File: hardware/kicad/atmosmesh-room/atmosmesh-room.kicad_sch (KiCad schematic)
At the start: 27 parts, among them U1 IDEASPARK_30PIN_PROVISIONAL

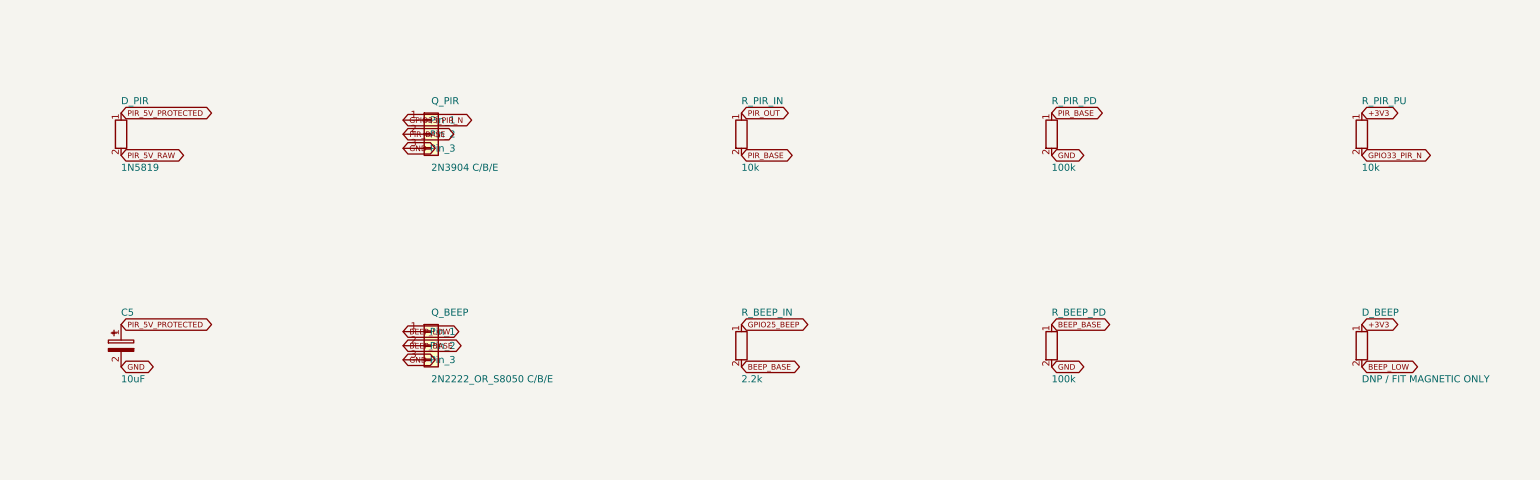
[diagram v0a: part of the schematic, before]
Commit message: :bug: fix(room): make the polarity symbols survive their own gates
The independent review asked for real polarity and C/B/E semantics so ERC can
catch a reversed diode or transistor. Fitting D_Schottky, D and Q_NPN_CBE and
adding per-instance descriptions did that, but left three gates red:

- The local library and the schematic's embedded copy were built from separate
  sources and given different Description text, so all 27 symbols raised
  lib_symbol_mismatch. Both now derive from the one list the schematic embeds,
  which also carries U1's passive pin types across.
- D_BEEP's new anode marker sits 7.62 mm right of the part origin and clipped
  mounting hole H2's mask at x=168. Moved to x=163.
- The .kicad_mod writer indents with spaces, so appending a literal tab to the
  marker continuation lines produced "space before tab" and failed task check.
  Continuation lines now extend the caller's own indent character.

Gates: ERC 0 violations, DRC 0 violations and 0 schematic-parity problems,
structural validation PASS, git diff --check clean. The 52 unconnected items
remain the intentional unrouted ratsnest. generate_project.py reproduces every
artifact byte-identically.
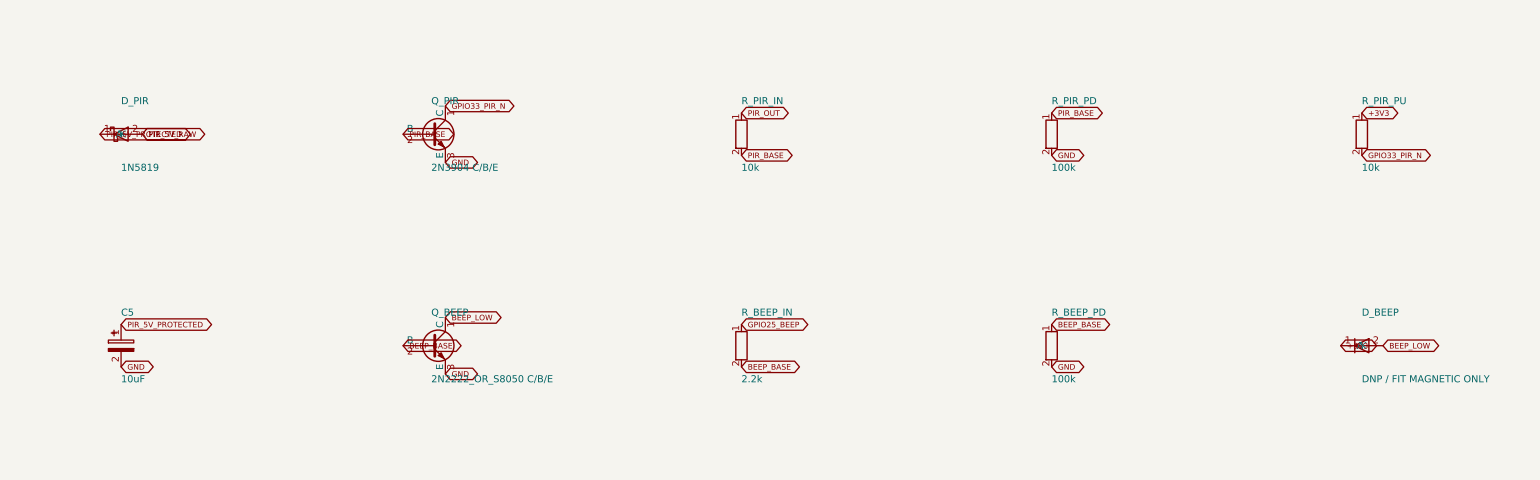
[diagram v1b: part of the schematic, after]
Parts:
- D_BEEP: symbol atmosmesh:R -> atmosmesh:D
- D_PIR: symbol atmosmesh:R -> atmosmesh:D_Schottky
- Q_BEEP, Q_PIR: symbol atmosmesh:Conn_01x03 -> atmosmesh:Q_NPN_CBE

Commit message: :sparkles: feat(room): build against the board the operator actually has
The controller is the ideaspark ESP32 1.14 inch TFT LCD board, confirmed from
docs/hardware/ideaspark-esp32-tft-pinout.png. The design assumed an integrated
I2C OLED, and that assumption was load-bearing in three places.

Its display is SPI. GPIO21/22 carry no onboard device, so:

- D-022's rejection of a sensor-supply diode rested on the OLED holding SDA/SCL
  at 3.3 V. That reason was false here. The decision is unchanged, on the real
  reason: every pull-up references the same rail the sensors run from.
- Nothing pulls the bus up. D-023 adds R_PU_SDA/R_PU_SCL 4k7 as required parts,
  on the sensor side of the 330R series resistors.
- GPIO23/18/15/2/4/32 belong to the display, GPIO12 is the flash strap and
  GPIO1/3 are the USB-UART. D-024 puts them off-limits behind a generator guard
  and a validator assertion.

U1's socket map was provisional and wrong in almost every position: pad 7 held
GPIO33 where the board has GPIO26, pad 30 held 3V3 where the board has GPIO23.
Rebuilt from a named pin table. Knowing the pin order makes the socket more
dangerous, not less, so the reserved pins are silkscreened too.

Operator also confirmed two module orders that were wrong on the carrier:

- SHT41 is VIN/GND/SCL/SDA; the carrier had SDA and SCL crossed.
- D-SUN PIR is GND/OUT/VCC; the carrier order would have put 5 V on the
  module's ground pin.

Gates: ERC 0, DRC 0 violations and 0 parity problems, structural validation
PASS, git diff --check clean. Both new gates mutation-proved: mapping GPIO23
raises in the generator, a rogue GPIO18 net fails the validator, and dropping
R_PU_SDA fails the pull-up assertion.

Still unverified: the physical row spacing, and both 5 V modules' supply
voltage and output swing.
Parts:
- added R_PU_SCL, R_PU_SDA: 4.7k, room:R_Axial_P7.62mm, symbol atmosmesh:R
- J_PIR: value DSUN_PIR -> DSUN_PIR GND/OUT/VCC
- J_SHT: value SHT41_3V3 -> SHT41 VIN/GND/SCL/SDA
- U1: value IDEASPARK_30PIN_PROVISIONAL -> IDEASPARK_ESP32_1V14_TFT_30PIN
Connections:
- net +3V3: now also U1.16 (GPIO23), R_PU_SCL.2, R_PU_SDA.2; no longer U1.30 (3V3)
- net +5V_USB_CONFIRMED: now also U1.1 (EN); no longer U1.15 (VIN)
- net GND: now also J_PIR.1 (Pin_1), U1.17 (GPIO22), U1.2 (GPIO36/VP); no longer J_PIR.2 (Pin_2), U1.14 (GND), U1.29 (GND)
- net GPIO21_SDA: now also U1.26 (GPIO4); no longer U1.20 (GPIO21)
- net GPIO22_SCL: now also U1.29 (GND); no longer U1.17 (GPIO22)
- net GPIO33_PIR_N: now also U1.9 (GPIO26); no longer U1.7 (GPIO33)
- net PIR_5V_PROTECTED: now also J_PIR.3 (Pin_3); no longer J_PIR.1 (Pin_1)
- net PIR_OUT: now also J_PIR.2 (Pin_2); no longer J_PIR.3 (Pin_3)
- net SCL_EXT: now also J_SHT.3 (Pin_3), R_PU_SCL.1; no longer J_SHT.4 (Pin_4)
- net SDA_EXT: now also J_SHT.4 (Pin_4), R_PU_SDA.1; no longer J_SHT.3 (Pin_3)
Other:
- note added: "DO NOT FABRICATE - IDEASPARK PIN NAMES CONFIRMED; ROW SPACING + MODULE PINOUTS STILL UNVERIFIED"
- note added: "Display is SPI, not I2C: GPIO21/22 carry no onboard device. R_PU_SDA/R_PU_SCL 4k7 are the only bus pullups."
- note added: "NEVER WIRE: GPIO23/18/15/2/4/32 drive the 1.14in TFT; GPIO12 is the flash strap; GPIO1/3 are the USB-UART."
- note removed: "DO NOT FABRICATE - VERIFY EXACT IDEASPARK BOARD / 30-PIN ROW SPACING / FRONT + BACK PHOTOS"
- note removed: "Onboard OLED stays directly on GPIO21/GPIO22. External sensors are behind 330R series resistors."
- moved on the sheet: C1, C2, C3, C4, TP_3V3, TP_5V, TP_GND, TP_SCL, TP_SDA

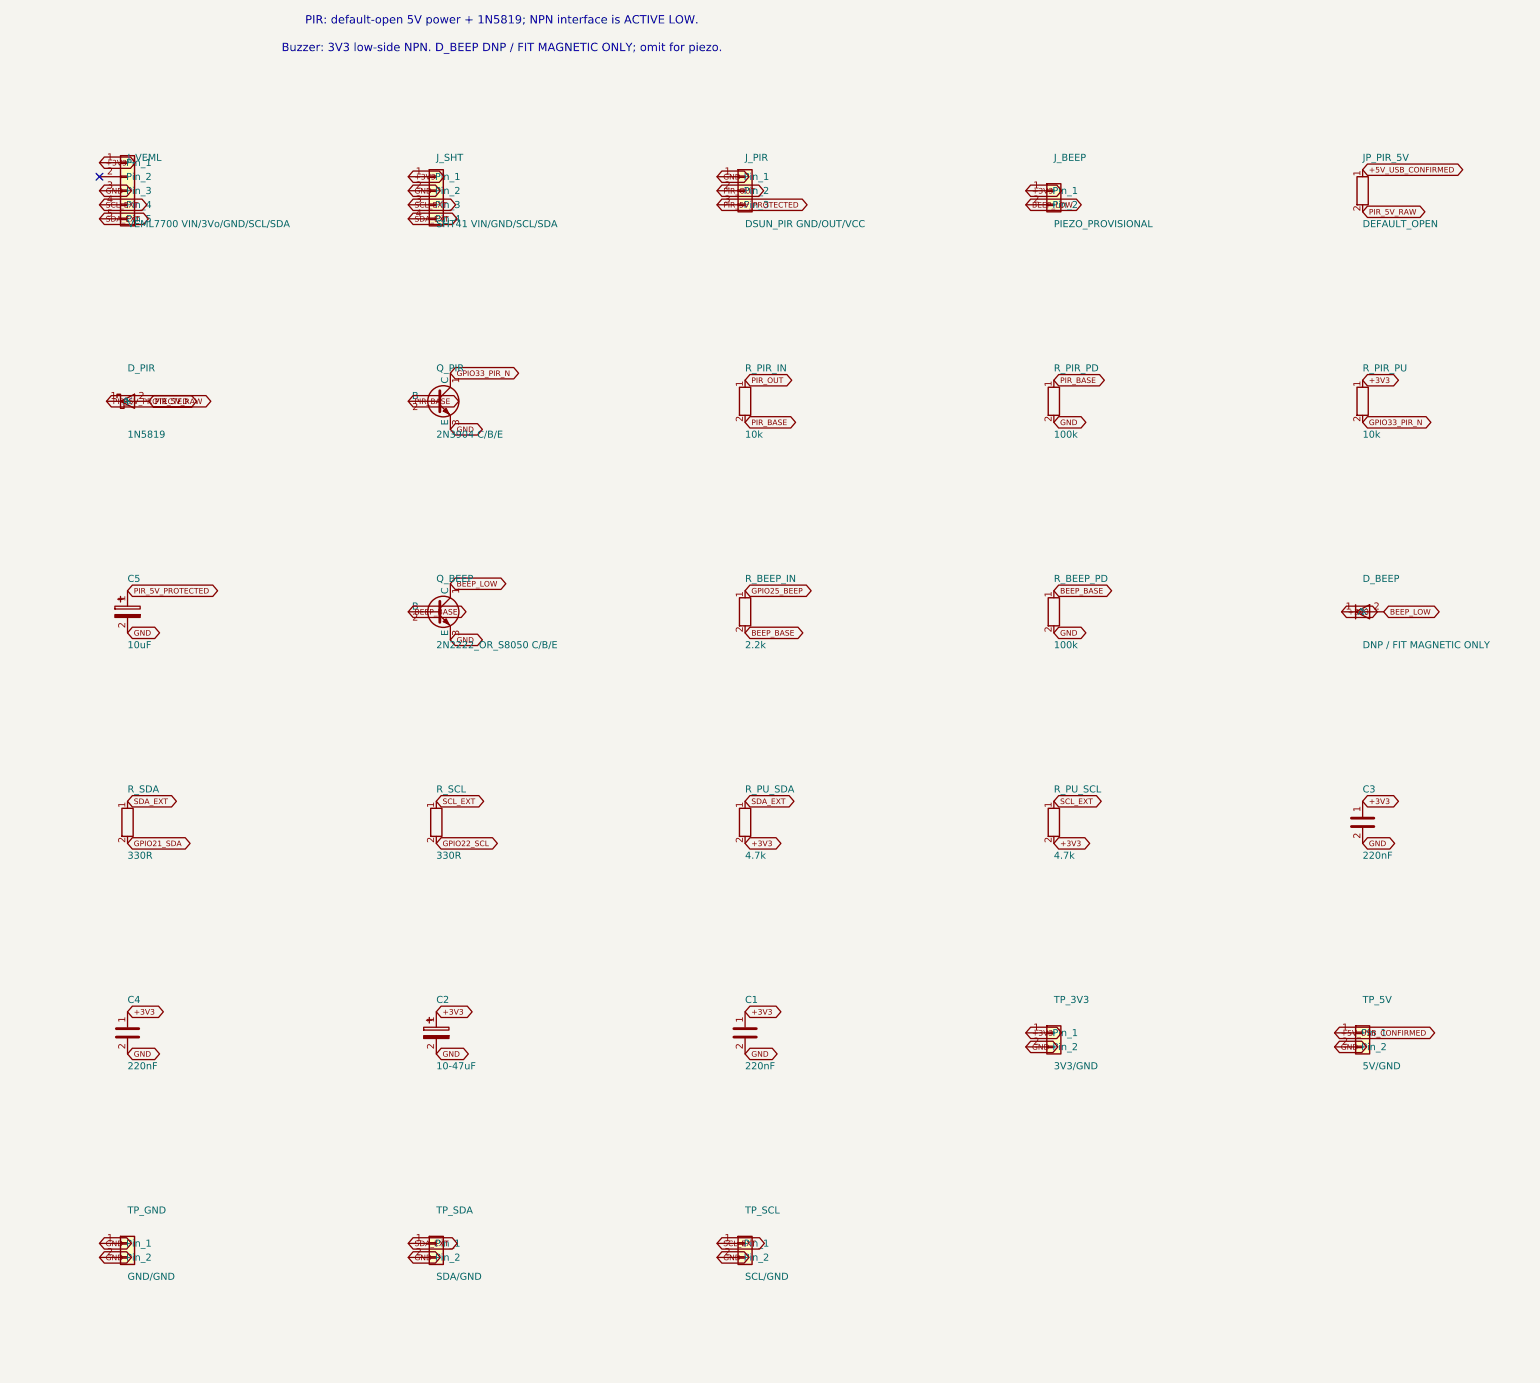
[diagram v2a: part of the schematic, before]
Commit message: :bug: fix(room): wire the buzzer the module actually has
Operator identified it: a no-name Keyes 3-pin breakout, black cylinder with a
single hole, header order S / VCC / -. It is the same part AtmosMesh v1 uses,
and firmware/README.md records v1 driving it with a bare 50 ms
digitalWrite(HIGH) on GPIO25. So it is an active module with its own driver.

The carrier presented a 2-pin header and switched the load's low side. Against
a 3-pin S/VCC/- module that could not have worked at all: the module's S input
had no connection. Q_BEEP, R_BEEP_IN, R_BEEP_PD and the D_BEEP flyback are
removed. GPIO25 now drives S through R_BEEP_S 100R, active HIGH, matching v1.
No flyback is fitted because an internally-driven module keeps the inductive
kick behind its own transistor.

R_BEEP_S starts at the protective value on purpose. Some Keyes buzzer boards
put the sounder straight across S and - with no onboard transistor, and 100R
would make such a module barely click. The bench rule is to measure rather than
to drive harder: only a measured current under 20 mA authorises a wire link.

ROOM-01's low-side-NPN acceptance criterion is marked superseded rather than
rewritten, and the reasoning is recorded as D-025.

Gates: ERC 0, DRC 0 violations and 0 parity problems, structural validation
PASS, git diff --check clean. The validator now asserts BEEP_BASE and BEEP_LOW
are absent, so the old driver cannot come back unnoticed.
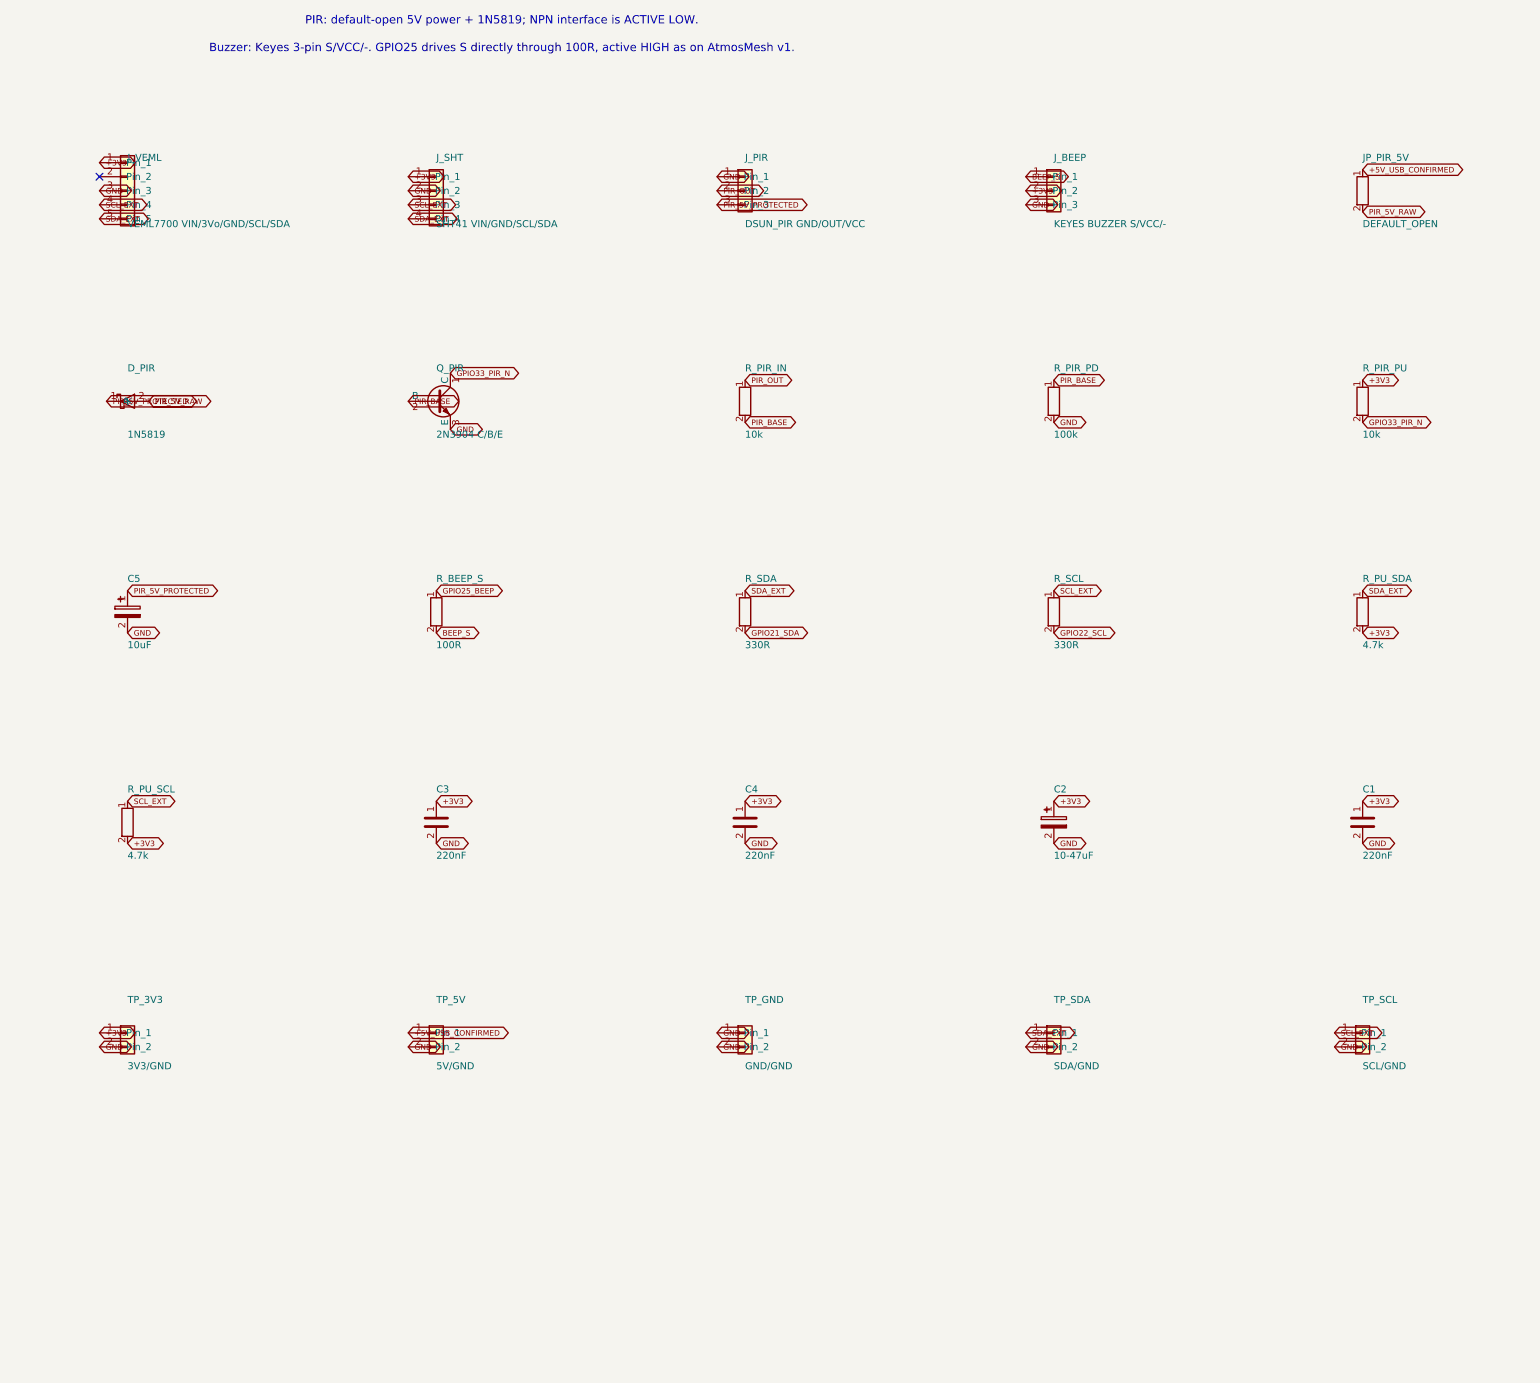
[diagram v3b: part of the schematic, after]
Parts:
- removed D_BEEP: DNP / FIT MAGNETIC ONLY, room:D_Axial_P7.62mm, symbol atmosmesh:D
- removed Q_BEEP: 2N2222_OR_S8050 C/B/E, room:TO92_CBE, symbol atmosmesh:Q_NPN_CBE
- removed R_BEEP_IN: 2.2k, room:R_Axial_P7.62mm, symbol atmosmesh:R
- removed R_BEEP_PD: 100k, room:R_Axial_P7.62mm, symbol atmosmesh:R
- added R_BEEP_S: 100R, room:R_Axial_P7.62mm, symbol atmosmesh:R
- J_BEEP: value PIEZO_PROVISIONAL -> KEYES BUZZER S/VCC/-; footprint room:PinHeader_1x02_P2.54mm -> room:PinHeader_1x03_P2.54mm; symbol atmosmesh:Conn_01x02 -> atmosmesh:Conn_01x03
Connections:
- net BEEP_LOW is gone; now on net +3V3: J_BEEP.2 (Pin_2)
- net +3V3: no longer J_BEEP.1 (Pin_1)
- net GND: now also J_BEEP.3 (Pin_3)
- net GPIO25_BEEP: now also R_BEEP_S.1
- new net BEEP_S: J_BEEP.1 (Pin_1), R_BEEP_S.2
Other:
- note added: "Buzzer: Keyes 3-pin S/VCC/-. GPIO25 drives S directly through 100R, active HIGH as on AtmosMesh v1."
- note removed: "Buzzer: 3V3 low-side NPN. D_BEEP DNP / FIT MAGNETIC ONLY; omit for piezo."
- moved on the sheet: C1, C2, C3, C4, R_PU_SCL, R_PU_SDA, R_SCL, R_SDA, TP_3V3, TP_5V, TP_GND, TP_SCL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
